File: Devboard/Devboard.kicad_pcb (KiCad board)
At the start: 2 copper layers, 33.8 x 75.3 mm, 36 parts, among them J1 USB_C_Receptacle_USB2.0_14P, J2 Conn_01x20, J3 Conn_01x20, J4 Conn_01x03, SW1 SW_Push, SW2 SW_Push, U1 RP2040, U2 MCP1700x-120xxMB, U3 W25Q128JVS, U4 ER_OLEDM0.91_1x-I2C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

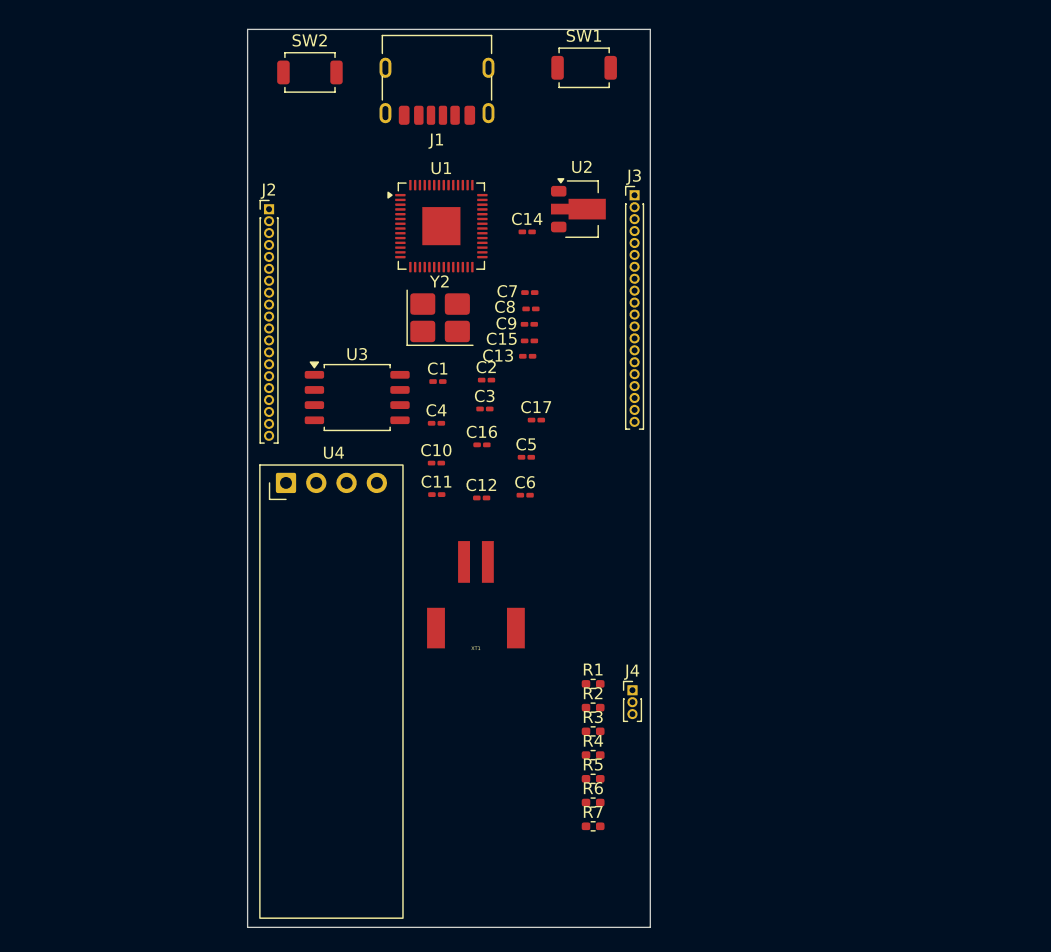
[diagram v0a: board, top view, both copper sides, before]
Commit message: Worked on routing
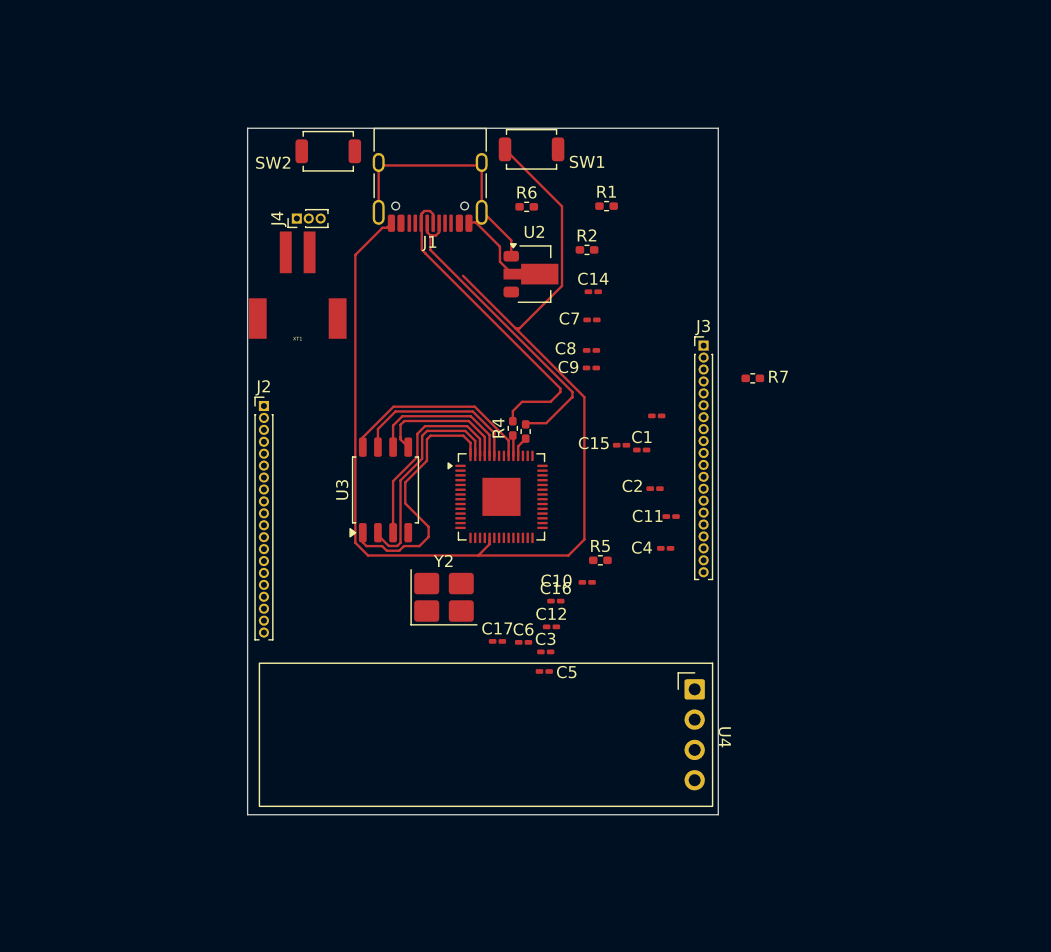
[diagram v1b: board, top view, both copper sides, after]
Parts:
- J1: footprint Connector_USB:USB_C_Receptacle_HRO_TYPE-C-31-M-17 -> Connector_USB:USB_C_Receptacle_HRO_TYPE-C-31-M-12
- Y2: value Crystal -> Crystal_GND24
- moved R6 50.3 mm to (143.9, 55.2)
- moved J4 48.5 mm to (124.6, 56.2), turned to 90 degrees
- moved R1 40.1 mm to (150.6, 55.1)
- moved R7 39.9 mm to (162.9, 69.6)
- moved U4 38.4 mm to (158.0, 95.7), turned to -90 degrees
- moved R2 38.4 mm to (149.0, 58.8)
- moved XT1 30.0 mm to (124.7, 66.3)
- moved R4 28.2 mm to (142.8, 73.8), turned to 90 degrees
- moved R3 25.8 mm to (143.8, 74.0), turned to 90 degrees
- moved Y2 23.4 mm to (137.0, 88.0)
- moved U1 23.3 mm to (141.8, 79.5)
- moved C4 21.9 mm to (155.6, 83.8)
- moved C3 21.0 mm to (145.5, 92.5)
- moved C11 19.7 mm to (156.0, 81.2)
- moved C17 18.8 mm to (141.5, 91.7)
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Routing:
- net GPIO6: track 0.00 -> 116.6 mm
- net USB D+: track 0.00 -> 28.1 mm
- net USB D-: track 0.00 -> 26.1 mm
- net QSPI_SS: track 0.00 -> 22.2 mm
- net QSPI_SD1: track 0.00 -> 18.5 mm
- net +3V3: track 0.00 -> 16.6 mm
- net QSPI_SD2: track 0.00 -> 16.5 mm
- net QSPI_SD3: track 0.00 -> 14.6 mm
- net QSPI_SCLK: track 0.00 -> 12.6 mm
- net QSPI_SDO: track 0.00 -> 11.5 mm
- net VBUS: track 0.00 -> 7.04 mm
- net Net-(U1-USB_DP): track 0.00 -> 1.73 mm
- net Net-(U1-USB_DM): track 0.00 -> 1.71 mm
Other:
- board size 33.8 x 75.3 mm -> 39.5 x 57.6 mm

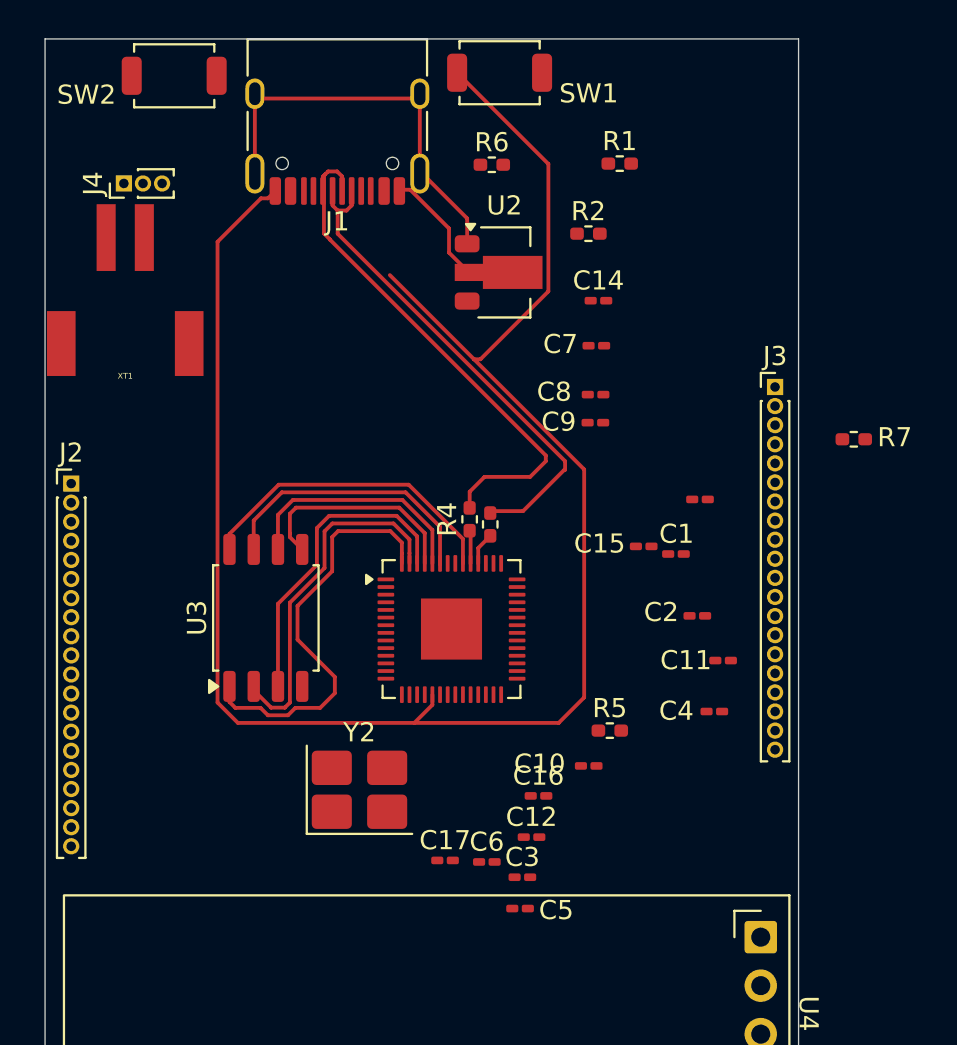
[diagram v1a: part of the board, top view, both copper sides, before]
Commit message: Routed the pins more.
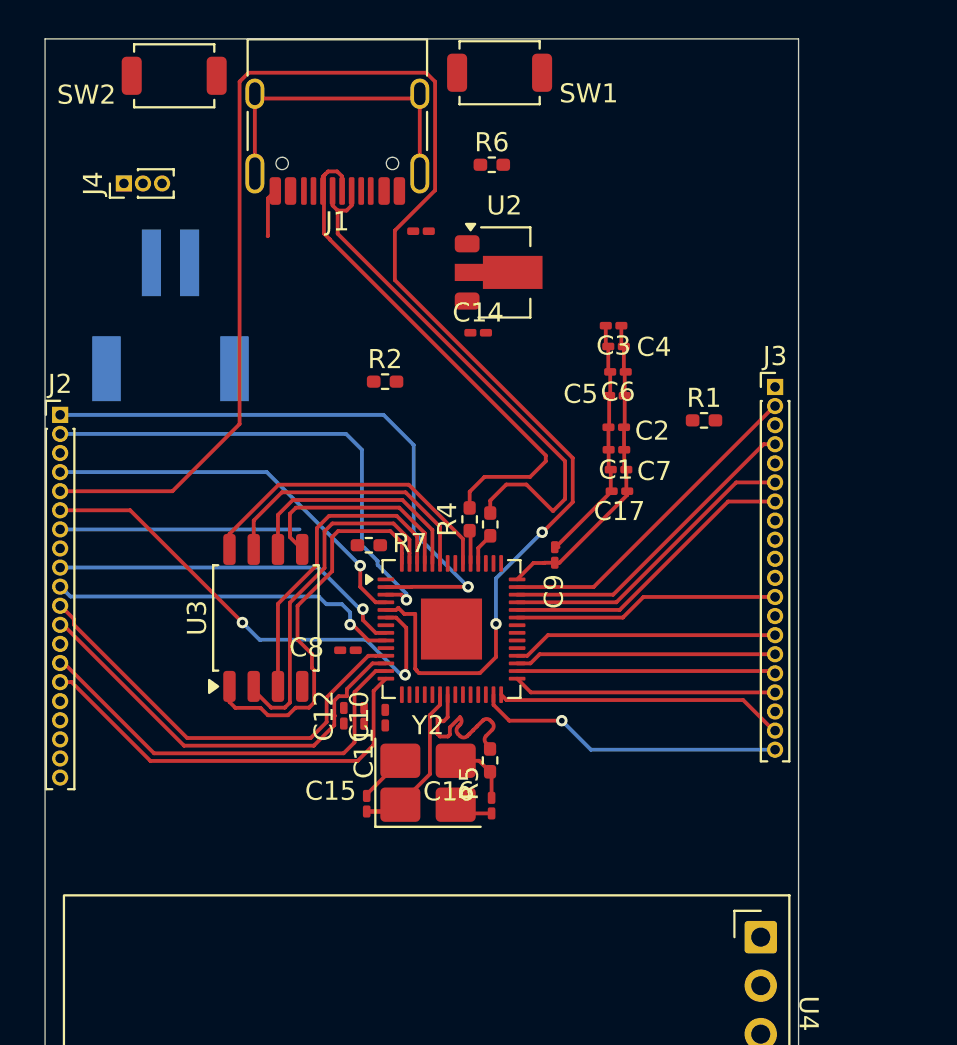
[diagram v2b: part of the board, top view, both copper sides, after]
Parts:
- XT1: moved to B.Cu
- moved C3 29.3 mm to (150.3, 63.6), turned to 180 degrees
- moved C5 27.3 mm to (150.5, 67.3), turned to 180 degrees
- moved C6 26.6 mm to (150.5, 66.1), turned to 180 degrees
- moved R7 26.0 mm to (137.5, 75.1)
- moved C17 21.4 mm to (150.6, 72.3), turned to 180 degrees
- moved C13 20.3 mm to (140.2, 58.7)
- moved C15 19.8 mm to (137.4, 88.7), turned to -90 degrees
- moved C4 19.8 mm to (150.4, 64.7), turned to 180 degrees
- moved C11 19.0 mm to (137.2, 84.1), turned to 90 degrees
- moved C8 18.6 mm to (136.4, 80.6)
- moved R1 14.2 mm to (155.0, 68.6)
- moved R2 13.2 mm to (138.3, 66.6)
- moved C12 11.7 mm to (136.2, 84.1), turned to 90 degrees
- moved C10 11.0 mm to (138.3, 84.2), turned to 90 degrees
- moved C2 10.8 mm to (150.4, 69.0), turned to 180 degrees
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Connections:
- C1 pad 2: GPIO6 -> GND
- C10 pad 2: GPIO6 -> GND
- C11 pad 2: GPIO6 -> GND
- C12 pad 2: GPIO6 -> GND
- C13 pad 2: GPIO6 -> GND
- C14 pad 1: GPIO6 -> GND
- C15 pad 1: GPIO6 -> GND
- C16 pad 1: GPIO6 -> GND
- C17 pad 2: GPIO6 -> GND
- C2 pad 2: GPIO6 -> GND
- C3 pad 2: GPIO6 -> GND
- C4 pad 2: GPIO6 -> GND
- C5 pad 2: GPIO6 -> GND
- C6 pad 2: GPIO6 -> GND
- C7 pad 2: GPIO6 -> GND
- C8 pad 2: GPIO6 -> GND
- C9 pad 2: GPIO6 -> GND
- J1 pad A1: GPIO6 -> GND
- J1 pad A12: GPIO6 -> GND
- J1 pad B1: GPIO6 -> GND
- J1 pad B12: GPIO6 -> GND
- J1 pad SH: GPIO6 -> GND
- J2 pad 13: GPIO6 -> GND
- J2 pad 18: GPIO6 -> GND
- J2 pad 3: GPIO6 -> GND
- J2 pad 7: GPIO5 -> unconnected-(J2-Pin_7-Pad7)
- J2 pad 8: GPIO6 -> GND
- J2 pad 9: unconnected-(J2-Pin_9-Pad9) -> GPIO6
- J3 pad 12: unconnected-(J3-Pin_12-Pad12) -> GPIO25
- J3 pad 13: GPIO6 -> GND
- J3 pad 18: GPIO6 -> GND
- J3 pad 3: GPIO6 -> GND
- J3 pad 8: GPIO6 -> GND
- J4 pad 2: GPIO6 -> GND
- R1 pad 2: GPIO6 -> GND
- R2 pad 2: GPIO6 -> GND
- SW1 pad 1: GPIO6 -> GND
- SW2 pad 2: GPIO6 -> GND
- U1 pad 1: Net-(U1-ADC_AVDD) -> +3V3
- U1 pad 10: Net-(U1-ADC_AVDD) -> +3V3
- U1 pad 19: GPIO6 -> GND
- U1 pad 22: Net-(U1-ADC_AVDD) -> +3V3
- U1 pad 33: Net-(U1-ADC_AVDD) -> +3V3
- U1 pad 37: unconnected-(U1-GPIO25-Pad37) -> GPIO25
- U1 pad 42: Net-(U1-ADC_AVDD) -> +3V3
- U1 pad 43: Net-(U1-ADC_AVDD) -> +3V3
- U1 pad 44: Net-(U1-ADC_AVDD) -> +3V3
- U1 pad 49: Net-(U1-ADC_AVDD) -> +3V3
- U1 pad 57: GPIO6 -> GND
- U1 pad 7: GPIO5 -> unconnected-(U1-GPIO5-Pad7)
- U2 pad 1: GPIO6 -> GND
- U3 pad 4: GPIO6 -> GND
- U4 pad 1: GPIO6 -> GND
- XT1 pad 2: GPIO6 -> GND
- Y2 pad 2: GPIO6 -> GND
- Y2 pad 4: GPIO6 -> GND
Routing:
- net GPIO6: track 116.6 -> 18.8 mm, vias 0 -> 1
- net GPIO3: track 0.00 -> 85.3 mm, vias 0 -> 2
- net GND: track 0.00 -> 37.2 mm
- net GPIO0: track 0.00 -> 32.1 mm, vias 0 -> 1
- net GPIO1: track 0.00 -> 26.2 mm, vias 0 -> 1
- net GPIO4: track 0.00 -> 25.4 mm, vias 0 -> 2
- net GPIO8: track 0.00 -> 22.8 mm
- net GPIO9: track 0.00 -> 22.5 mm
- net GPIO10: track 0.00 -> 22.3 mm
- net GPIO11: track 0.00 -> 22.2 mm
- net GPIO2: track 0.00 -> 20.5 mm, vias 0 -> 1
- net GPIO7: track 0.00 -> 18.6 mm, vias 0 -> 1
- net GPIO29: track 0.00 -> 17.4 mm
- net GPIO28: track 0.00 -> 16.8 mm
- net +3V3: track 16.6 -> 33.2 mm
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
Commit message: Worked on routing the PCB more
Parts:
- moved J4 35.7 mm to (121.7, 91.7), turned to 180 degrees
- moved R1 23.6 mm to (133.7, 58.5)
- moved R6 23.5 mm to (136.3, 77.4), turned to 90 degrees
- moved C12 11.3 mm to (125.4, 80.6)
- moved C11 11.1 mm to (126.7, 80.7)
- moved C10 10.9 mm to (128.0, 80.8)
- moved R2 8.82 mm to (132.5, 59.9)
- moved C13 1.89 mm to (138.3, 58.7), turned to 90 degrees
- moved C8 0.59 mm to (135.9, 81.0), turned to 180 degrees
- moved SW2 0.17 mm to (127.4, 50.5)
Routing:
- net VBUS: track 1.11 -> 77.2 mm, vias 0 -> 3
- net Net-(R6-Pad1): track 0.00 -> 59.5 mm, vias 0 -> 4
- net GPIO22: track 0.00 -> 51.8 mm, vias 0 -> 4
- net GPIO24: track 0.00 -> 47.1 mm, vias 0 -> 1
- net GPIO23: track 0.00 -> 45.9 mm, vias 0 -> 1
- net +3V3: track 33.2 -> 79.1 mm, vias 0 -> 4
- net SWCLK: track 0.00 -> 35.6 mm, vias 0 -> 1
- net SWD: track 0.00 -> 30.8 mm, vias 0 -> 1
- net GPIO14: track 0.00 -> 29.2 mm, vias 0 -> 1
- net GND: track 37.2 -> 64.6 mm, vias 0 -> 15
- net +1V1: track 0.00 -> 25.8 mm, vias 0 -> 2
- net GPIO15: track 0.00 -> 21.5 mm, vias 0 -> 2
- net GPIO13: track 0.00 -> 20.4 mm, vias 0 -> 1
- net GPIO12: track 0.00 -> 18.3 mm, vias 0 -> 1
- net Net-(J1-CC1): track 0.00 -> 7.57 mm, vias 0 -> 2
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- added copper zone on B.Cu, net GND
- added copper zone on F.Cu, net GND

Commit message: Worked on more routing
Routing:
- net GND: track 64.6 -> 94.5 mm, vias 15 -> 18
- net GPIO17: track 15.1 -> 18.4 mm
- net GPIO29: track 17.4 -> 19.7 mm
- net QSPI_SS: track 24.2 -> 25.6 mm, vias 0 -> 2

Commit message: Routing part 2 electric boogalooo
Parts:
- XT1: moved to F.Cu
- moved J4 39.1 mm to (158.1, 77.6), turned to 90 degrees
- moved XT1 36.1 mm to (163.0, 63.4), turned to 0 degrees
- moved R7 34.8 mm to (103.0, 70.3)
- moved C11 34.6 mm to (157.2, 64.5)
- moved R6 34.5 mm to (103.0, 68.3), turned to 0 degrees
- moved C12 32.9 mm to (154.0, 64.3)
- moved C10 28.5 mm to (156.2, 77.5), turned to -90 degrees
- moved C8 27.4 mm to (160.4, 68.6), turned to 0 degrees
- moved R1 26.3 mm to (159.8, 55.5), turned to -90 degrees
- moved SW2 25.3 mm to (151.4, 58.4)
- moved C13 22.9 mm to (161.1, 56.5), turned to -90 degrees
- moved R3 21.3 mm to (156.2, 56.7)
- moved R4 21.1 mm to (155.0, 56.6)
- moved U3 21.0 mm to (147.4, 64.5), turned to 0 degrees
- moved J1 20.0 mm to (155.6, 49.4)
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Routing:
- net GND: track 94.5 -> 0.00 mm, vias 18 -> 0
- net VBUS: track 77.4 -> 0.00 mm, vias 3 -> 0
- net +3V3: track 79.1 -> 154.5 mm, vias 4 -> 0
- net GPIO3: track 83.9 -> 14.1 mm, vias 2 -> 0
- net Net-(R6-Pad1): track 59.5 -> 0.00 mm, vias 4 -> 0
- net SWCLK: track 35.6 -> 3.54 mm, vias 1 -> 0
- net SWD: track 30.8 -> 5.00 mm, vias 1 -> 0
- net USB D-: track 28.7 -> 5.45 mm
- net USB D+: track 28.1 -> 5.36 mm
- net GPIO24: track 47.1 -> 27.9 mm, vias 1 -> 0
- net +1V1: track 25.8 -> 9.43 mm, vias 2 -> 0
- net GPIO0: track 32.8 -> 17.6 mm, vias 1 -> 0
- net unconnected-(J2-Pin_7-Pad7): track 12.5 -> 0.00 mm
- net GPIO4: track 25.4 -> 13.8 mm, vias 2 -> 0
- net GPIO8: track 22.8 -> 12.6 mm
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- removed copper zone on B.Cu, net GND
- removed copper zone on F.Cu, net GND
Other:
- board outline removed

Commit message: Lowk forgot to push yesterday but did more routing
yesterday I made ok progress. I need to move the pins tho
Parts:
- R1: moved to B.Cu
- moved R6 43.6 mm to (146.0, 60.9)
- moved R7 41.0 mm to (143.0, 61.3)
- moved R1 7.47 mm to (156.8, 48.7), turned to 0 degrees
- moved XT1 1.08 mm to (163.2, 62.4)
- moved R2 0.76 mm to (151.4, 56.1)
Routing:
- net VBUS: track 0.00 -> 92.0 mm, vias 0 -> 4
- net +3V3: track 154.5 -> 190.3 mm, vias 0 -> 1
- net +1V1: track 9.43 -> 41.9 mm, vias 0 -> 1
- net QSPI_SS: track 16.3 -> 22.0 mm
- net Net-(J1-CC1): track 0.00 -> 5.05 mm, vias 0 -> 1
- net Net-(R6-Pad1): track 0.00 -> 2.92 mm
- net Net-(U2-VO): track 0.00 -> 2.38 mm
- net GND: track 0.00 -> 1.45 mm
- net GPIO22: track 44.8 -> 45.7 mm
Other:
- board outline added: 38.7 x 47.5 mm

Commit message: Finished routing
A pretty productive day so far
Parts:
- R2: moved to B.Cu
- moved R2 7.86 mm to (153.9, 48.6), turned to 180 degrees
- moved C9 6.98 mm to (159.7, 66.7)
- moved J3 5.74 mm to (175.4, 63.2)
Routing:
- net GND: track 1.45 -> 117.9 mm, vias 0 -> 26
- net +3V3: track 190.3 -> 167.0 mm, vias 1 -> 3
- net +1V1: track 41.9 -> 50.6 mm, vias 1 -> 4
- net GPIO18: track 13.0 -> 18.8 mm
- net GPIO19: track 12.8 -> 18.5 mm
- net GPIO29: track 13.2 -> 18.9 mm
- net GPIO28: track 13.3 -> 19.1 mm
- net GPIO26: track 13.9 -> 19.6 mm
- net GPIO16: track 15.5 -> 21.2 mm
- net GPIO27: track 13.8 -> 19.6 mm
- net GPIO25: track 13.0 -> 18.8 mm
- net GPIO21: track 12.4 -> 18.1 mm
- net GPIO20: track 12.6 -> 18.4 mm
- net GPIO17: track 14.3 -> 20.1 mm
- net Net-(J1-CC2): track 0.00 -> 5.09 mm, vias 0 -> 1
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- added copper zone on B.Cu, net GND
- added copper zone on F.Cu, net GND
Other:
- board size 38.7 x 47.5 mm -> 38.7 x 50.6 mm

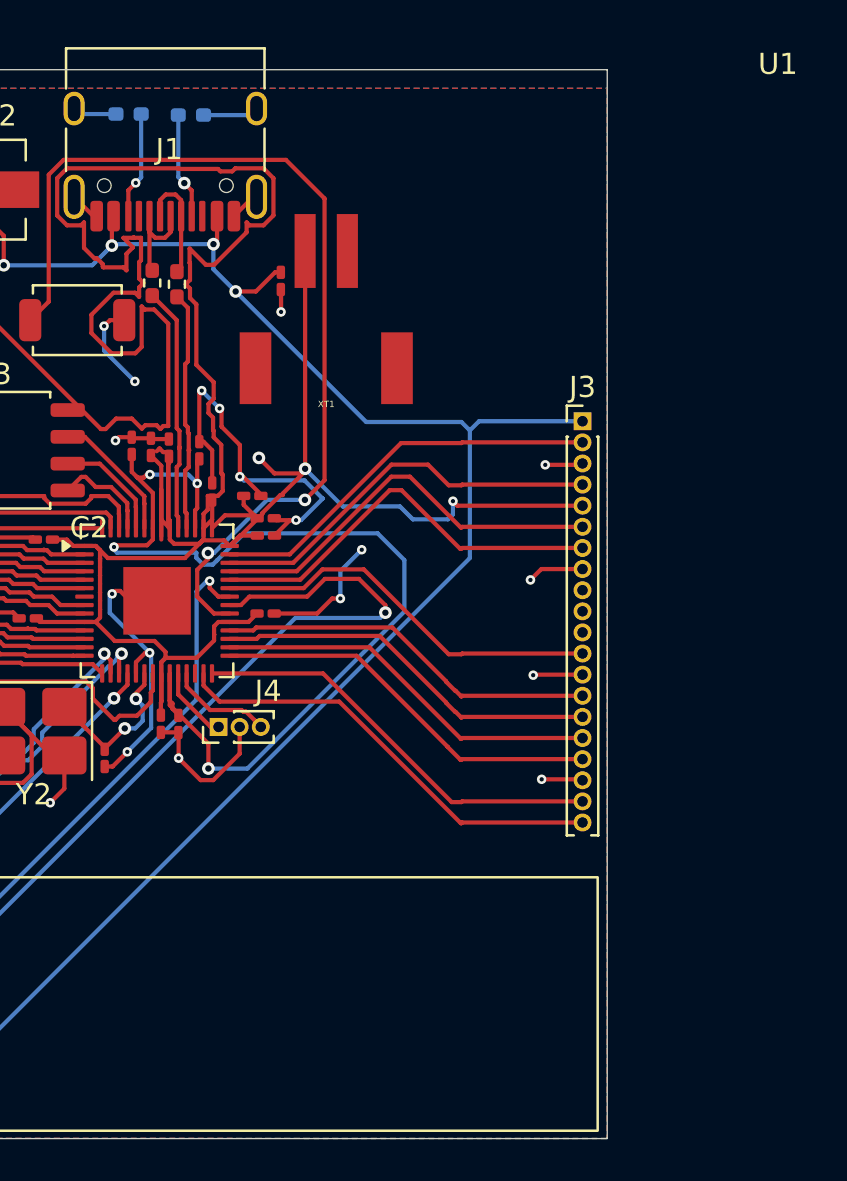
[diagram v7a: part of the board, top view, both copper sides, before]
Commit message: Worked on the art of devboard
Got the assets made and started to implement them.
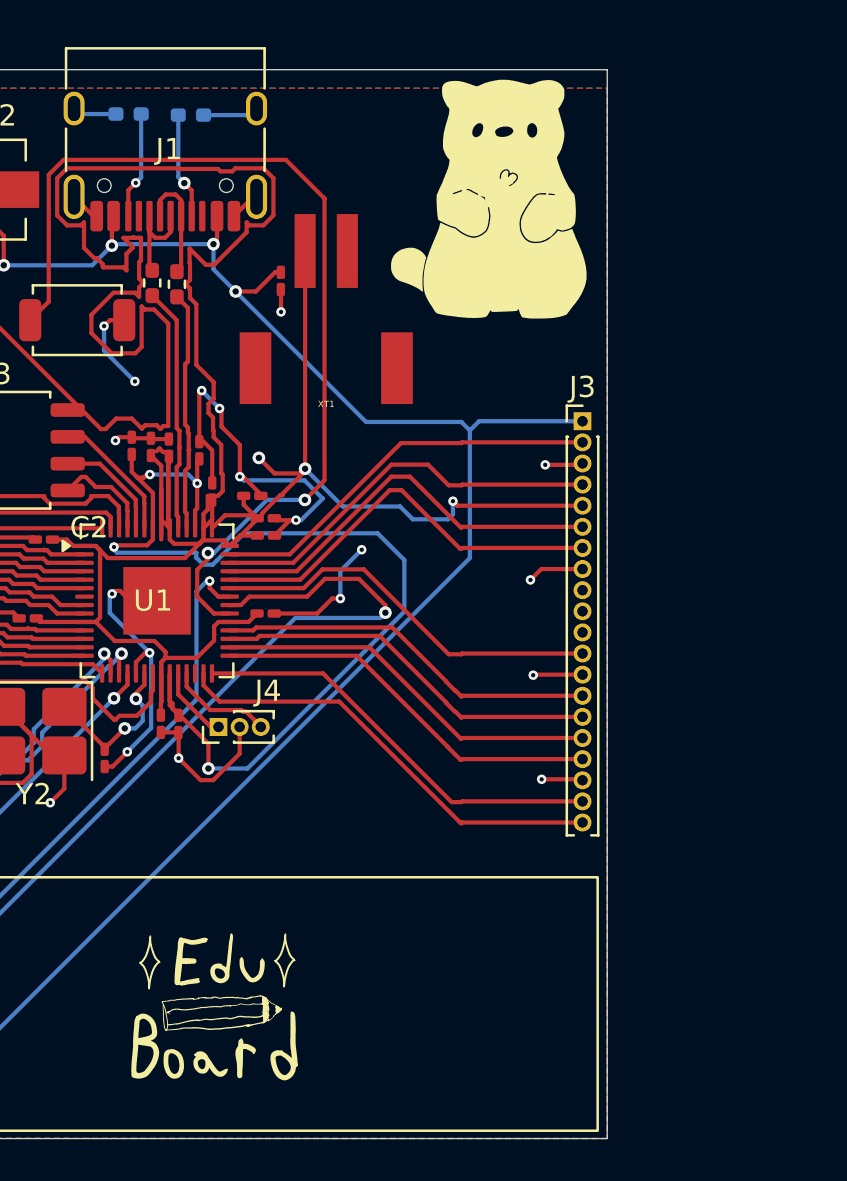
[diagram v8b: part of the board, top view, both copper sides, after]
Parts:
- added G***: LOGO, DevboardArt:SoupSmall, F.Cu at (171.9, 52.4)
- added G***: LOGO, DevboardArt:Sparkle, F.Cu at (171.6, 53.3)
